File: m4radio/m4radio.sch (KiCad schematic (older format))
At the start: 71 parts

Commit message: Use cusf-kicad.lib instead of agg-kicad.lib
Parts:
- C1, C10, C11, C12, C13, C14, C15, C16, C17, C18, C19, C2, C20, C21, C22, C23, C24, C25, C26, C27, C28, C29, C3, C30, C31, C32, C33, C4, C5, C6, C7, C8, C9: renamed from C?; symbol agg-kicad:C -> cusf-kicad:C
- D1, D2, D3: renamed from D?; symbol agg-kicad:LED -> cusf-kicad:LED
- D4, D5: renamed from D?; symbol agg-kicad:ESD_DIODE -> cusf-kicad:ESD_DIODE
- IC1: renamed from IC?; symbol agg-kicad:NCP4620 -> cusf-kicad:NCP4620
- IC10: renamed from IC?; symbol agg-kicad:Si4460 -> cusf-kicad:Si4460
- IC2: renamed from IC?; symbol agg-kicad:MCP2562 -> cusf-kicad:MCP2562
- IC3: renamed from IC?; symbol agg-kicad:STM32F405RxTx -> cusf-kicad:STM32F405RxTx
- IC4: renamed from IC?; symbol agg-kicad:MAX-M8Q -> cusf-kicad:MAX-M8Q
- IC5: renamed from IC?; symbol agg-kicad:NC7SZ04 -> cusf-kicad:NC7SZ04
- IC6: renamed from IC?; symbol agg-kicad:NCP380 -> cusf-kicad:NCP380
- IC7: renamed from IC?; symbol agg-kicad:CS2100-CP -> cusf-kicad:CS2100-CP
- IC8: renamed from IC?; symbol agg-kicad:SL18860DC -> cusf-kicad:SL18860DC
- IC9: renamed from IC?; symbol agg-kicad:SN74LVC1G0832 -> cusf-kicad:SN74LVC1G0832
- J1, J2: renamed from J?; symbol agg-kicad:CONN_02x15 -> cusf-kicad:CONN_02x15
- L1, L2, L3, L4, L5, L6, L7, L8: renamed from L?; symbol agg-kicad:L -> cusf-kicad:L
- P1: renamed from P?; symbol agg-kicad:SWD_TC -> cusf-kicad:SWD_TC
- P2, P3: renamed from P?; symbol agg-kicad:COAX -> cusf-kicad:COAX
- R1, R2, R3, R4, R5, R6, R7, R8, R9: renamed from R?; symbol agg-kicad:R -> cusf-kicad:R
- Y1: renamed from Y?; symbol agg-kicad:TCXO -> cusf-kicad:TCXO

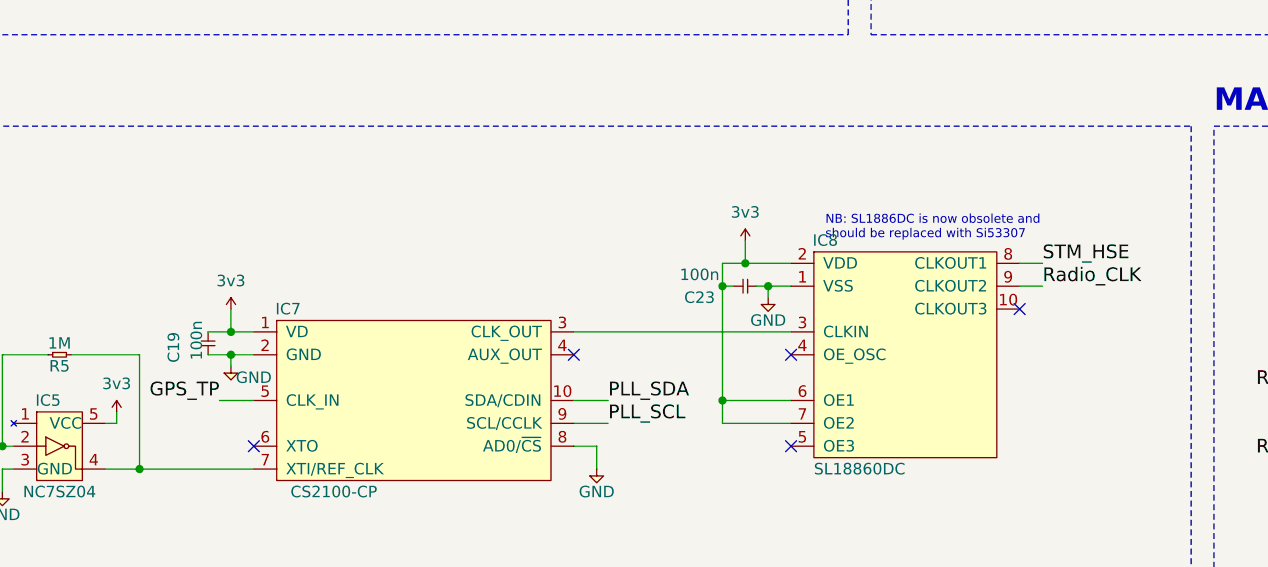
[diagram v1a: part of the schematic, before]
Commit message: Merge sd into dl, convert symbols to cusf-kicad, and add UART
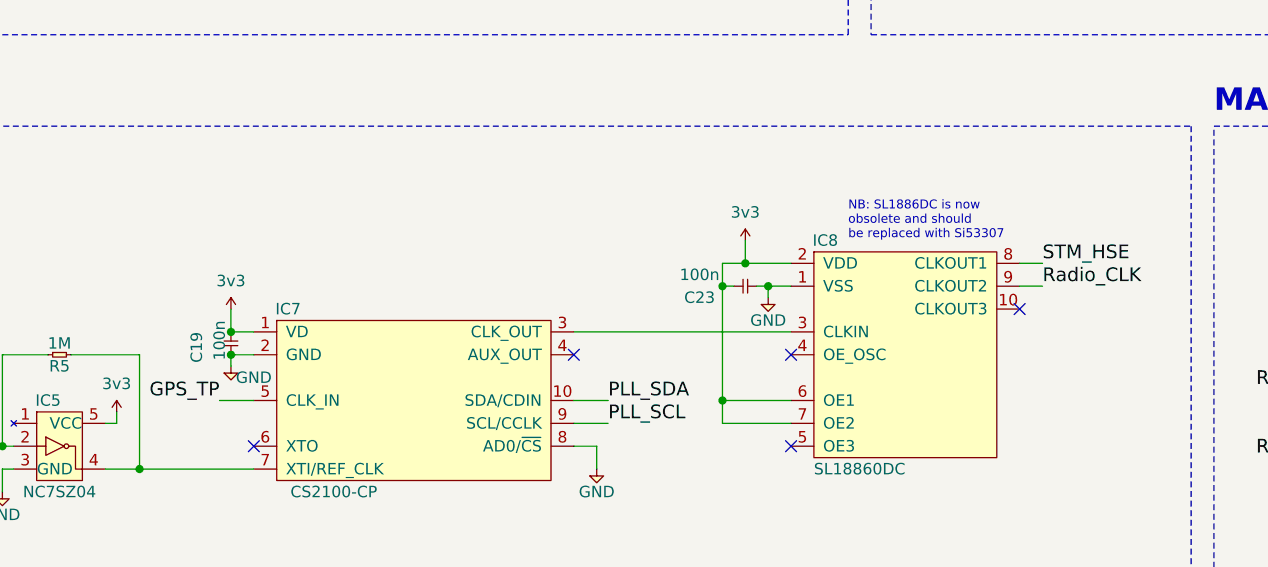
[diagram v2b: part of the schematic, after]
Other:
- note added: "NB: SL1886DC is now\nobsolete and should\nbe replaced with Si53307"
- note removed: "NB: SL1886DC is now obsolete and\nshould be replaced with Si53307"
- moved on the sheet: C19
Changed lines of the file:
@@
 EESchema Schematic File Version 4
-LIBS:m4radio-cache
 EELAYER 30 0
 EELAYER END
@@
 Connection ~ 7050 4350
 Wire Wire Line
-	7050 4350 6950 4350
-Wire Wire Line
 	7050 4400 7050 4350
 $Comp
 L cusf-kicad:C C19
 U 1 1 5E74F302
-P 6950 4350
-F 0 "C19" H 7050 4500 50  0000 R CNN
-F 1 "100n" H 7100 4400 50  0000 R CNN
-F 2 "" H 6950 4350 50  0001 C CNN
-F 3 "" H 6950 4350 50  0001 C CNN
-	1    6950 4350
+P 7050 4350
+F 0 "C19" H 7150 4500 50  0000 R CNN
+F 1 "100n" H 7200 4400 50  0000 R CNN
+F 2 "" H 7050 4350 50  0001 C CNN
+F 3 "" H 7050 4350 50  0001 C CNN
+	1    7050 4350
 	0    -1   -1   0
 $EndComp
-Wire Wire Line
-	6950 4250 7050 4250
 Wire Wire Line
 	7050 4250 7050 4150
@@
 NoConn ~ 1850 6800
 NoConn ~ 1850 6900
-Text Notes 9650 3850 0    39   ~ 0
-NB: SL1886DC is now obsolete and\nshould be replaced with Si53307
+Text Notes 9750 3850 0    39   ~ 0
+NB: SL1886DC is now\nobsolete and should\nbe replaced with Si53307
 $Comp
 L cusf-kicad:C C1
